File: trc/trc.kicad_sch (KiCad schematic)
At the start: 23 parts, among them J1 PWR, J2 Control, J3 Inverter, J4 BMS, J5 States, J6 Relays, SW1 EXT_FAULT_JUMPER

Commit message: Merged new-pcbs branch
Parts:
- removed D1: LED, LED_SMD:LED_0603_1608Metric, symbol Device:LED
- removed R1: 3k3, Resistor_SMD:R_0805_2012Metric_Pad1.20x1.40mm_HandSolder, symbol Device:R_Small
- removed R7, R8: 10k, Resistor_SMD:R_0805_2012Metric_Pad1.20x1.40mm_HandSolder, symbol Device:R_Small
- removed SW1: EXT_FAULT_JUMPER, Connector_PinHeader_2.54mm:PinHeader_1x03_P2.54mm_Vertical, symbol Switch:SW_SPDT
- added C10, C12, C7, C9: 100n, Capacitor_SMD:C_0805_2012Metric_Pad1.18x1.45mm_HandSolder, symbol Device:C_Small
- added R11, R12, R14: 10k, Resistor_SMD:R_0805_2012Metric_Pad1.20x1.40mm_HandSolder, symbol Device:R_Small
- D2: Order Code (none) -> 241-SS14W_R1_00001; Supplier (none) -> Mouser
- H1, H2, H3, H4: now left out of the parts list
- J1, J2, J3, J4, J6: footprint Connector_Molex:Molex_Micro-Fit_3.0_43045-0400_2x02_P3.00mm_Horizontal -> Connector_Molex:Molex_Micro-Fit_3.0_43045-0412_2x02_P3.00mm_Vertical; Order Code (none) -> 538-43045-0412; Supplier (none) -> Mouser
- J5: Order Code (none) -> 538-43045-0412; Supplier (none) -> Mouser
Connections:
- net TS_ENABLED is gone; now on net INV_CLOSE_PCHG_RLY: J3.1 (Pin_1)
- net ~{BMS_DISCHG_EN} is gone; now on net ~{CHG_EN_INTERLOCKED}: J4.1 (Pin_1)
- net CLOSE_NEG_AIR: no longer J5.4 (Pin_4)
- net CLOSE_PCHG_RLY: no longer J5.2 (Pin_2)
- net CLOSE_POS_AIR: no longer J5.3 (Pin_3)
- net Control Logic/TS_READY: now also J2.2 (Pin_2); no longer J5.1 (Pin_1)
- net GND: now also R5.2, C10.2, C12.2, C7.1, C9.1; no longer J4.3 (Pin_3), J4.4 (Pin_4), R3.2
- net INV_CLOSE_MAIN_CONTACTOR: now also J3.2 (Pin_2), R14.1; no longer J3.4 (Pin_4)
- net INV_CLOSE_PCHG_RLY: now also R12.1; no longer J3.2 (Pin_2)
- net TS_ON_INPUT: now also R5.1, R11.2; no longer R3.1
- net ~{CHG_EN_INTERLOCKED}: now also R2.2, R3.2; no longer J4.2 (Pin_2)
- removed net EXT_FAULT_INPUT: J2.2 (Pin_2), R5.2
- net INV_FAULT_INDICATOR: no longer names the net of J3.3 (Pin_3)
- net INV_FAULT_INDICATOR: no longer R2.2
- new net Control Logic/INV_CLOSE_MAIN_CONTACTOR: C7.2, R14.2
- new net Control Logic/INV_CLOSE_PCHG_RLY: C9.2, R12.2
- new net Control Logic/TS_ON_INPUT: C10.1, R11.1
- new net Control Logic/~{CHG_EN_INTERLOCKED}: C12.1, R3.1
- new net Control Logic/~{HIGH_AIR_INTENDED_ON}: J5.1 (Pin_1)
- new net Control Logic/~{LOW_AIR_INTENDED_ON}: J5.2 (Pin_2)
- new net Control Logic/~{PRCHG_INTENDED_ON}: J5.3 (Pin_3)
- no-connect marks 0 -> 6
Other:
- sheet Control Logic ports: added CHG_EN_NEG_AIR, CHG_EN_POS_AIR, SHUTDOWN, ~{HIGH_AIR_INTENDED_ON}, ~{LOW_AIR_INTENDED_ON}, ~{PRCHG_INTENDED_ON}; removed CHG_EN, EXT_FAULT, TS_ENABLED, ~{DISCHG_EN}, ~{INV_FAULT}
- sheet Relays ports: added CHG_EN_NEG_AIR, CHG_EN_POS_AIR; removed CHG_EN
- note added: "150Hz cutoff"
- note added: "If the INTENDED_* signals are to work with the SHDN loop open (as required for TSAL), they must be supplied separately from SHDN_IN. This means the TRC needs a 12V supply."
- note added: "Pin 1 connects to a "charging interlock" which may only be installed when the TSAC is outside the car. The goal here is to make it impossible for the AIRs to accidentally be closed by the charge enable signal when the TSAC is inside the car. Under no circumstances should ~{CHG_EN_INTERLOCKED} be connected at the same time as the inverter!"
- note added: "Time constant 1ms rise, 2ms fall (through pull-down resistor). Asymmetry not ideal, but not a problem because the signals are slow."
- note removed: "Pins 2 connects to a "charging interlock" which may only be installed when the TSAC is outside the car. The goal here is to make it impossible for the AIRs to accidentally be closed by the charge enable signal when the TSAC is inside the car. Under no circumstances should ~{CHG_EN_INTERLOCKED} be connected at the same time as the inverter!"
- note removed: "TRC TODO: - Filters - Test stability of 12V - Ground return path for whole shutdown loop?"
- note removed: "The EXT fault input is an active high external fault source, in case we ever need it. When used, the jumper (switch) should be set to pull up so that if the input is disconnected, it faults. When unused, the jumper should be set to pull down ("always OK")."
- note removed: "The fault indicator blinks a fault code by providing a ground connection The signal is latched low by the control logic to handle blinking, opening the AIRs and pre-charge relay The inverter will also command the +AIR and pre-charge relay open in a fault condition, so this is more a redundancy"
- moved on the sheet: C1, D2, F1, H1, H2, H3, H4, J1, J2, J3, J4, J5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

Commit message: Revert "Merge branch 'main' into dash"
This reverts commit b6cdca404b12c725dd5b2429809eeaf13edaa5f0, reversing
changes made to 1ff41de2af88940e740711c3ca966c3c5c3adf12.
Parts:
- removed C12: 100n, Capacitor_SMD:C_0805_2012Metric_Pad1.18x1.45mm_HandSolder, symbol Device:C_Small
- removed J1: PWR, Connector_Molex:Molex_Micro-Fit_3.0_43045-0412_2x02_P3.00mm_Vertical, symbol Connector_Generic:Conn_01x04
- removed J2: Control, Connector_Molex:Molex_Micro-Fit_3.0_43045-0412_2x02_P3.00mm_Vertical, symbol Connector_Generic:Conn_01x04
- removed J3: Inverter, Connector_Molex:Molex_Micro-Fit_3.0_43045-0412_2x02_P3.00mm_Vertical, symbol Connector_Generic:Conn_01x04
- removed J4: BMS, Connector_Molex:Molex_Micro-Fit_3.0_43045-0412_2x02_P3.00mm_Vertical, symbol Connector_Generic:Conn_01x04
- removed J5: States, Connector_Molex:Molex_Micro-Fit_3.0_43045-0412_2x02_P3.00mm_Vertical, symbol Connector_Generic:Conn_01x04
- removed J6: Relays, Connector_Molex:Molex_Micro-Fit_3.0_43045-0412_2x02_P3.00mm_Vertical, symbol Connector_Generic:Conn_01x04
- removed R2, R3: 10k, Resistor_SMD:R_0805_2012Metric_Pad1.20x1.40mm_HandSolder, symbol Device:R_Small
- added C2: 100u, Capacitor_THT:CP_Radial_D5.0mm_P2.00mm, symbol Device:C_Polarized
- added C4, C5, C7: 100n, Capacitor_SMD:C_0805_2012Metric_Pad1.18x1.45mm_HandSolder, symbol Device:C
- added F1: 0448.500MR, Fuse:Fuse_Littelfuse-NANO2-451_453, symbol Device:Fuse
- added J1, J2: Conn_01x12_Socket, Connector_Molex:Molex_Micro-Fit_3.0_43045-1200_2x06_P3.00mm_Horizontal, symbol Connector:Conn_01x12_Socket
- added R1, R10, R11, R2, R3, R4, R6, R7: 270, Resistor_SMD:R_2512_6332Metric, symbol Device:R
- added R13, R16, R17, R18: 10k, Resistor_SMD:R_0805_2012Metric_Pad1.20x1.40mm_HandSolder, symbol Device:R
- renumbered C7 to C3, C9 to C6, C10 to C8, C1 to C9, D2 to D1, F1 to F2, R6 to R12, R12 to R14, R14 to R15, R5 to R19, R11 to R20, R4 to R9
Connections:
- net +12V: now also R1.1, R10.1, R13.1, R3.1, R6.1
- net GND: now also C2.2, C4.2, C5.2, C7.2, J1.4 (Pin_4), J1.5 (Pin_5), J1.6 (Pin_6), J2.1 (Pin_1), J2.9 (Pin_9)
- net INV_CLOSE_MAIN_CONTACTOR: now also J2.8 (Pin_8)
- net INV_CLOSE_PCHG_RLY: now also J2.2 (Pin_2)
- net NEG_AIR: now also J2.11 (Pin_11)
- net PCHG_RLY+: now also J2.5 (Pin_5)
- net PCHG_RLY-: now also J2.4 (Pin_4)
- net POS_AIR: now also J2.12 (Pin_12)
- net SHDN_IN: now also J2.10 (Pin_10)
- net TS_ON_INPUT: now also J1.7 (Pin_7)
- new net: R1.2, R2.1, R3.2, R4.1
- new net: R10.2, R11.1, R6.2, R7.1
- new net +12VT: C2.1, F1.2
- new net GREEN_LED_ON: J1.8 (Pin_8)
- new net TSAL_POWER: F1.1, J2.7 (Pin_7)
- new net TS_READY: J1.2 (Pin_2)
- new net ~{HIGH_AIR_MECH_ON_IN}: J1.10 (Pin_10), R11.2, R17.2, R7.2
- new net ~{HIGH_AIR_MECH_ON}: C5.1, R17.1
- new net ~{LOW_AIR_MECH_ON_IN}: J1.9 (Pin_9), R16.2, R2.2, R4.2
- new net ~{LOW_AIR_MECH_ON}: C7.1, R16.1
- new net ~{PRCHG_MECH_ON_IN}: J1.11 (Pin_11), R13.2, R18.2
- new net ~{PRCHG_MECH_ON}: C4.1, R18.1
- new net ~{TS.DETECTED}: J1.1 (Pin_1)
- no-connect marks 6 -> 4
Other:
- sheet Control Logic ports: added GREEN_LED_ON, ~{HIGH_AIR_MECH_ON}, ~{LOW_AIR_MECH_ON}, ~{PRCHG_MECH_ON}, ~{TSAC_HV_DETECTED}; removed CHG_EN_NEG_AIR, CHG_EN_POS_AIR, ~{CHG_EN_INTERLOCKED}, ~{HIGH_AIR_INTENDED_ON}, ~{LOW_AIR_INTENDED_ON}, ~{PRCHG_INTENDED_ON}
- sheet Relays ports: added none; removed CHG_EN_NEG_AIR, CHG_EN_POS_AIR
- note added: "0.53W total, 0.13W each, use 2W resistors"
- note added: "Auxiliary contacts need a "wetting current" to prevent issues with contact oxidation in the long term (debatably) AIRs (EV200HAANA) : 100mA, here 44mA Pre-charge(GV222BAB) : 0.1mA @ 5V, here 1.2mA"
- note added: "Auxillary contacts (AIRs and precharge)"
- note added: "Charging logic will be controlled by the charger, with TS_ON being controlled by a switch and both INV signals being high, since the precharge board controls the high air"
- note added: "Electrolytics rated 26v Will need to bodge 2.5mm radial on if go to car 24v"
- note added: "Go to tsal and ground box"
- note added: "Intended relay states These are the voltages driving the coils Weakly pulled down for SCS"
- note added: "Will we need shutdown on two pins anyway to help with contact resistance"
- note removed: "BMS outputs are all open drain so must be pulled up"
- note removed: "Don't need 4 pins, but less parts to stock"
- note removed: "Pin 1 connects to a "charging interlock" which may only be installed when the TSAC is outside the car. The goal here is to make it impossible for the AIRs to accidentally be closed by the charge enable signal when the TSAC is inside the car. Under no circumstances should ~{CHG_EN_INTERLOCKED} be connected at the same time as the inverter!"
- moved on the sheet: C3, C6, C8, C9, D1, F2, H1, H2, H3, H4, R12, R14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

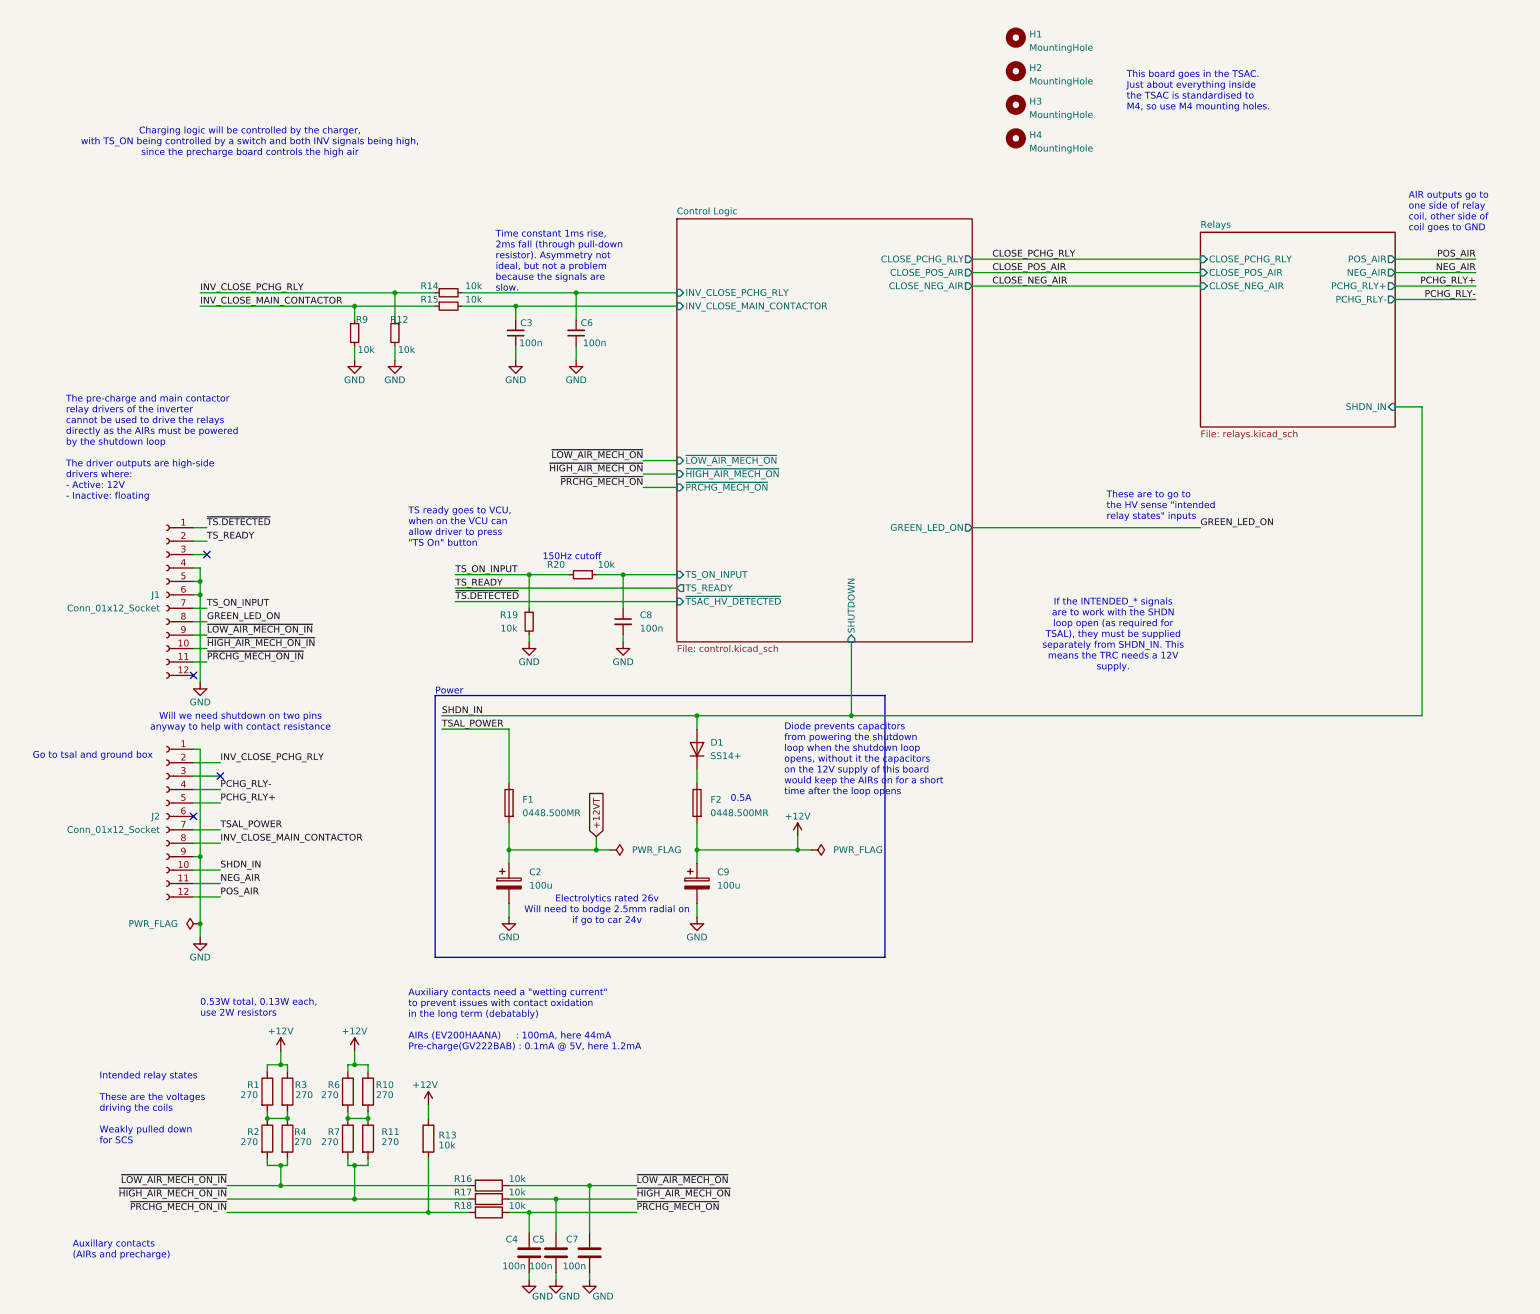
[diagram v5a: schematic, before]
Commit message: TSAL LED Release
* start of tsal LED design

there is nothing here

* Add files via upload

* Add files via upload

* New project filepaths, updated libraries

* lockfiles my beloved

* Updated to correct schematic

* PCB design 40%

* Added inductor, finialised board layout

* Simulations!

* Simulations were attempted

It was not fine

* Updated to take EN signal instead of TSAL sink

* RELEASE YAY

* Revert "Merge branch 'main' into tsal-led"

This reverts commit b8431bf9aab271a0ae3b7bb2565335d31a772841, reversing
changes made to 2533238e78a0882b7119c906f24b373fa21a2f26.

---------

Co-authored-by: f1lthyc4sualz <104178648+f1lthyc4sualz@users.noreply.github.com>
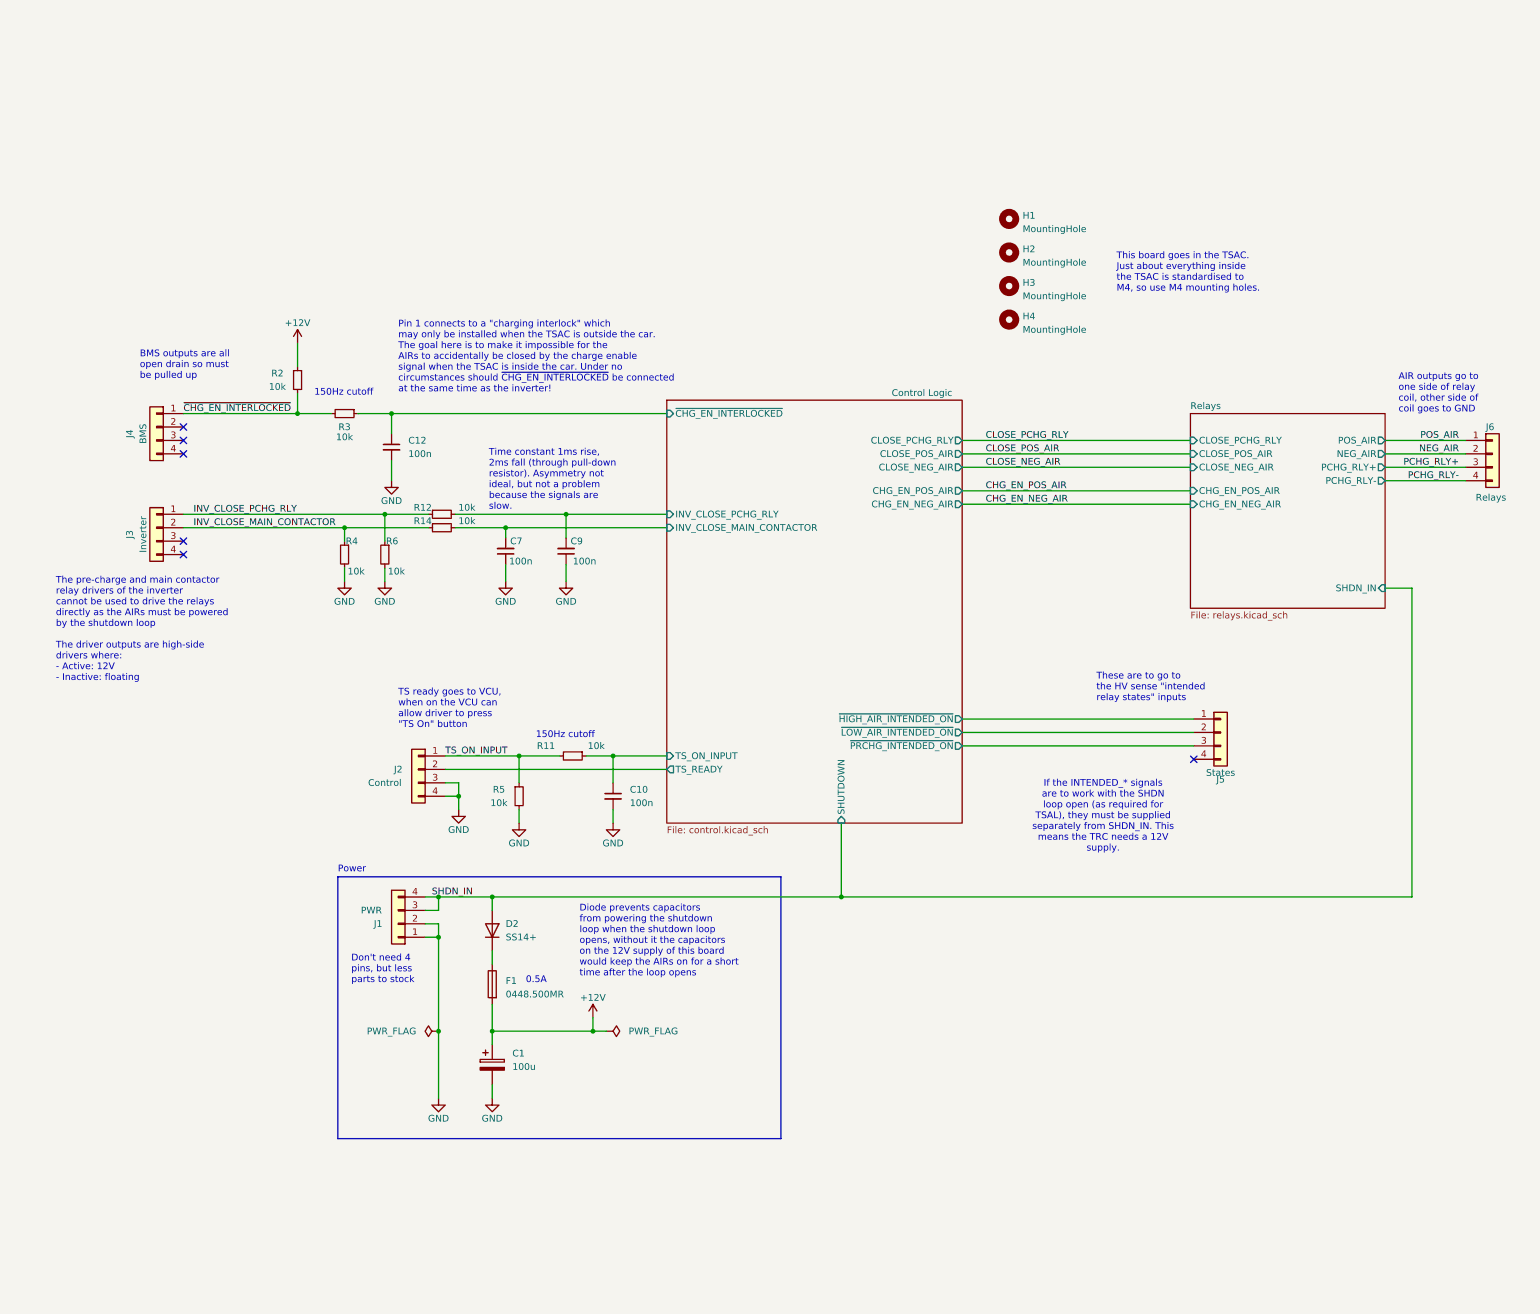
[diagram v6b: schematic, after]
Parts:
- removed C2: 100u, Capacitor_THT:CP_Radial_D5.0mm_P2.00mm, symbol Device:C_Polarized
- removed C4, C5, C7: 100n, Capacitor_SMD:C_0805_2012Metric_Pad1.18x1.45mm_HandSolder, symbol Device:C
- removed F1: 0448.500MR, Fuse:Fuse_Littelfuse-NANO2-451_453, symbol Device:Fuse
- removed J1, J2: Conn_01x12_Socket, Connector_Molex:Molex_Micro-Fit_3.0_43045-1200_2x06_P3.00mm_Horizontal, symbol Connector:Conn_01x12_Socket
- removed R1, R10, R11, R2, R3, R4, R6, R7: 270, Resistor_SMD:R_2512_6332Metric, symbol Device:R
- removed R13, R16, R17, R18: 10k, Resistor_SMD:R_0805_2012Metric_Pad1.20x1.40mm_HandSolder, symbol Device:R
- added C12: 100n, Capacitor_SMD:C_0805_2012Metric_Pad1.18x1.45mm_HandSolder, symbol Device:C_Small
- added J1: PWR, Connector_Molex:Molex_Micro-Fit_3.0_43045-0412_2x02_P3.00mm_Vertical, symbol Connector_Generic:Conn_01x04
- added J2: Control, Connector_Molex:Molex_Micro-Fit_3.0_43045-0412_2x02_P3.00mm_Vertical, symbol Connector_Generic:Conn_01x04
- added J3: Inverter, Connector_Molex:Molex_Micro-Fit_3.0_43045-0412_2x02_P3.00mm_Vertical, symbol Connector_Generic:Conn_01x04
- added J4: BMS, Connector_Molex:Molex_Micro-Fit_3.0_43045-0412_2x02_P3.00mm_Vertical, symbol Connector_Generic:Conn_01x04
- added J5: States, Connector_Molex:Molex_Micro-Fit_3.0_43045-0412_2x02_P3.00mm_Vertical, symbol Connector_Generic:Conn_01x04
- added J6: Relays, Connector_Molex:Molex_Micro-Fit_3.0_43045-0412_2x02_P3.00mm_Vertical, symbol Connector_Generic:Conn_01x04
- added R2, R3: 10k, Resistor_SMD:R_0805_2012Metric_Pad1.20x1.40mm_HandSolder, symbol Device:R_Small
- renumbered C9 to C1, C8 to C10, C3 to C7, C6 to C9, D1 to D2, F2 to F1, R20 to R11, R14 to R12, R15 to R14, R9 to R4, R19 to R5, R12 to R6
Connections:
- net +12V: now also R2.1
- net GND: now also C12.2, J1.1 (Pin_1), J1.2 (Pin_2), J2.3 (Pin_3), J2.4 (Pin_4)
- net INV_CLOSE_MAIN_CONTACTOR: now also J3.2 (Pin_2)
- net INV_CLOSE_PCHG_RLY: now also J3.1 (Pin_1)
- net NEG_AIR: now also J6.2 (Pin_2)
- net PCHG_RLY+: now also J6.3 (Pin_3)
- net PCHG_RLY-: now also J6.4 (Pin_4)
- net POS_AIR: now also J6.1 (Pin_1)
- net SHDN_IN: now also J1.3 (Pin_3), J1.4 (Pin_4)
- net TS_ON_INPUT: now also J2.1 (Pin_1)
- new net Control Logic/TS_READY: J2.2 (Pin_2)
- new net Control Logic/~{CHG_EN_INTERLOCKED}: C12.1, R3.1
- new net Control Logic/~{HIGH_AIR_INTENDED_ON}: J5.1 (Pin_1)
- new net Control Logic/~{LOW_AIR_INTENDED_ON}: J5.2 (Pin_2)
- new net Control Logic/~{PRCHG_INTENDED_ON}: J5.3 (Pin_3)
- new net ~{CHG_EN_INTERLOCKED}: J4.1 (Pin_1), R2.2, R3.2
- no-connect marks 4 -> 6
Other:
- sheet Control Logic ports: added CHG_EN_NEG_AIR, CHG_EN_POS_AIR, ~{CHG_EN_INTERLOCKED}, ~{HIGH_AIR_INTENDED_ON}, ~{LOW_AIR_INTENDED_ON}, ~{PRCHG_INTENDED_ON}; removed GREEN_LED_ON, ~{HIGH_AIR_MECH_ON}, ~{LOW_AIR_MECH_ON}, ~{PRCHG_MECH_ON}, ~{TSAC_HV_DETECTED}
- sheet Relays ports: added CHG_EN_NEG_AIR, CHG_EN_POS_AIR; removed none
- note added: "BMS outputs are all open drain so must be pulled up"
- note added: "Don't need 4 pins, but less parts to stock"
- note added: "Pin 1 connects to a "charging interlock" which may only be installed when the TSAC is outside the car. The goal here is to make it impossible for the AIRs to accidentally be closed by the charge enable signal when the TSAC is inside the car. Under no circumstances should ~{CHG_EN_INTERLOCKED} be connected at the same time as the inverter!"
- note removed: "0.53W total, 0.13W each, use 2W resistors"
- note removed: "Auxiliary contacts need a "wetting current" to prevent issues with contact oxidation in the long term (debatably) AIRs (EV200HAANA) : 100mA, here 44mA Pre-charge(GV222BAB) : 0.1mA @ 5V, here 1.2mA"
- note removed: "Auxillary contacts (AIRs and precharge)"
- note removed: "Charging logic will be controlled by the charger, with TS_ON being controlled by a switch and both INV signals being high, since the precharge board controls the high air"
- note removed: "Electrolytics rated 26v Will need to bodge 2.5mm radial on if go to car 24v"
- note removed: "Go to tsal and ground box"
- note removed: "Intended relay states These are the voltages driving the coils Weakly pulled down for SCS"
- note removed: "Will we need shutdown on two pins anyway to help with contact resistance"
- moved on the sheet: C1, C10, C7, C9, D2, F1, H1, H2, H3, H4, R11, R12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
